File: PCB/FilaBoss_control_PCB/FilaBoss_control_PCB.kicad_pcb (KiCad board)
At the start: 2 copper layers, 81.3 x 53.3 mm, 23 parts, among them J1 Conn_01x04_Encoder, J2 JST_2mm_LiPo, J3 JST_2mm_LiPo, J5 Barrel_Jack_SMD, J6 PinHeader_01x06_P2.54mm_Verti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, J7 Conn_01x04, J8 JST_2mm_3, J9 Conn_01x04_Encoder, Q1 IRLZ44N, Q2 IRLZ44N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

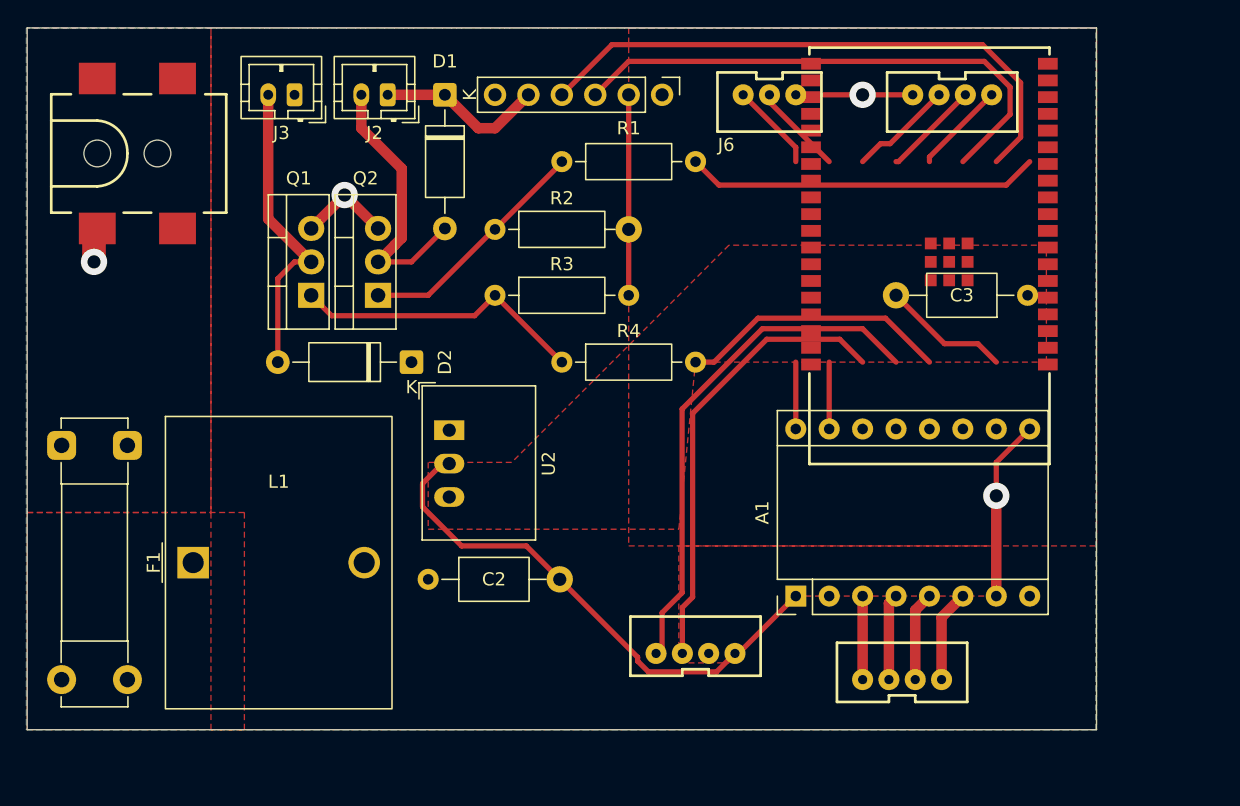
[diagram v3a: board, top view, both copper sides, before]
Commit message: pcb converted to esp32 wroom
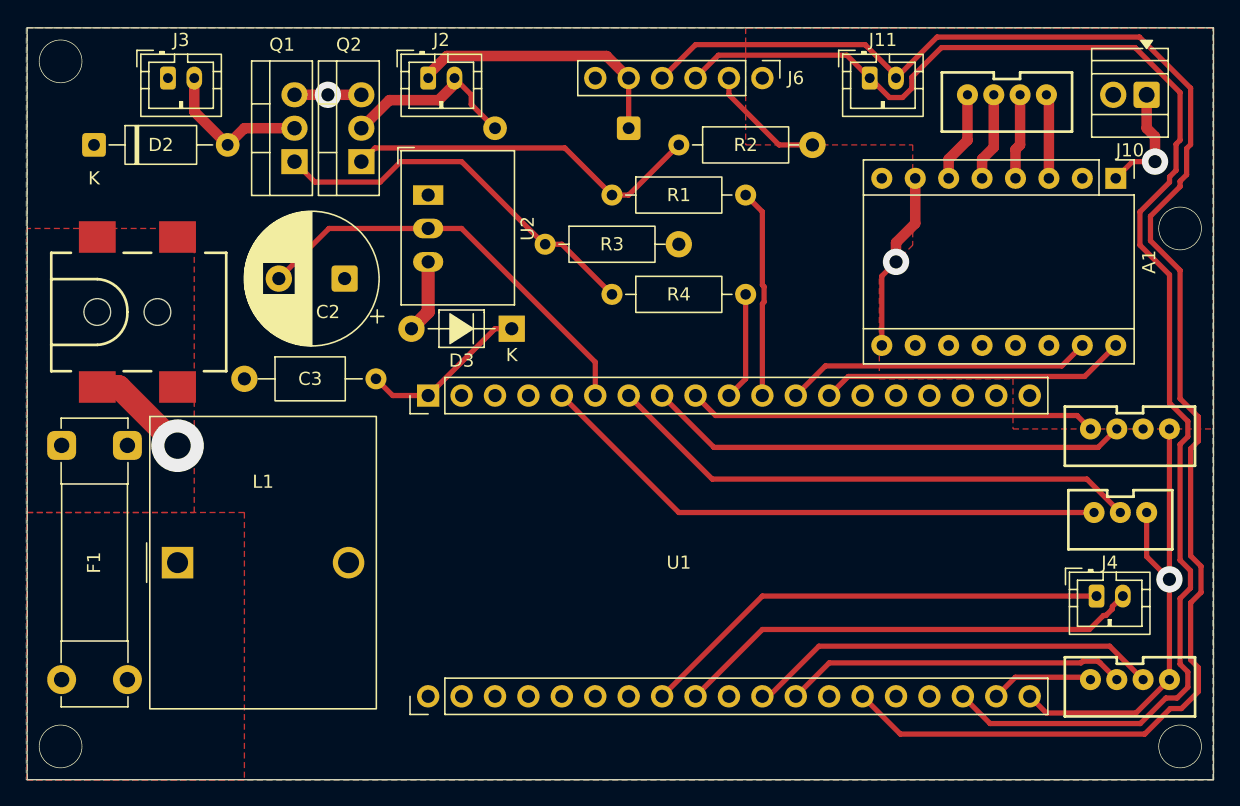
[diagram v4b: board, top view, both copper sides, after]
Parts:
- added D3: SB020, PCM_Diode_THT_AKL:D_T-1_P7.62mm_Horizontal, F.Cu at (74.9, 109.2)
- added J10: Screw_Terminal_01x02, TerminalBlock:TerminalBlock_Xinya_XY308-2.54-2P_1x02_P2.54mm_Horizontal, F.Cu at (123.2, 91.4)
- added J11: SCL/SDA, Connector_JST:JST_PH_B2B-PH-K_1x02_P2.00mm_Vertical, F.Cu at (102.1, 90.2)
- added J4: RX/TX, Connector_JST:JST_PH_B2B-PH-K_1x02_P2.00mm_Vertical, F.Cu at (119.4, 129.5)
- C2: footprint Capacitor_THT:C_Axial_L5.1mm_D3.1mm_P10.00mm_Horizontal -> Capacitor_THT:CP_Radial_D10.0mm_P5.00mm
- D1: moved to B.Cu
- J2: value JST_2mm_LiPo -> SPOOL
- J3: value JST_2mm_LiPo -> PULLER
- J9: value Conn_01x04_Encoder -> Conn_01x04_Pot
- U1: value ESP32-WROVER-E-N16R8 -> ~; footprint PCM_SparkFun-RF:ESP32-WROVER-E-IE -> custom:ESP32 Wroom dev-kit
- moved C3 59.9 mm to (54.6, 113.0), turned to 0 degrees
- moved J9 46.5 mm to (121.9, 136.4)
- moved J7 44.1 mm to (112.6, 92.0), turned to 180 degrees
- moved J8 41.5 mm to (121.2, 123.7)
- moved A1 40.0 mm to (120.8, 97.8), turned to -90 degrees
- moved J1 36.7 mm to (121.9, 117.4), turned to 180 degrees
- moved D2 29.2 mm to (43.2, 95.2), turned to 0 degrees
- moved C2 23.7 mm to (62.2, 105.4), turned to 180 degrees
- moved U2 17.9 mm to (68.6, 99.1)
- moved R2 15.4 mm to (87.6, 95.2)
- moved D1 14.2 mm to (83.8, 94.0), turned to 180 degrees
- moved U1 12.7 mm to (114.3, 114.3)
- moved J5 12.0 mm to (43.4, 108.0)
- moved Q1 10.2 mm to (58.4, 96.5)
- moved Q2 10.2 mm to (63.5, 96.5)
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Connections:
- A1 pad 15: unconnected-(A1-STEP-Pad15) -> Net-(A1-STEP)
- A1 pad 16: GND -> Net-(A1-DIR)
- C3 pad 1: +5V -> GND
- C3 pad 2: unconnected-(C3-Pad2) -> +5V
- J1 pad 1: unconnected-(J1-Pin_1-Pad1) -> GND
- J1 pad 2: unconnected-(J1-Pin_2-Pad2) -> +3.3V
- J1 pad 3: +3.3V -> Net-(J1-Pin_3)
- J1 pad 4: GND -> Net-(J1-Pin_4)
- J6 pad 3: Net-(J6-Pin_3) -> Net-(J11--)
- J6 pad 4: unconnected-(J6-Pin_4-Pad4) -> Net-(J11-+)
- J8 pad 2: unconnected-(J8-Pad2) -> Net-(U1-GPIO12)
- J8 pad 3: unconnected-(J8-Pad3) -> Net-(U1-GPIO13)
- J9 pad 1: Net-(J9-Pin_1) -> GND
- J9 pad 4: GND -> Net-(J9-Pin_4)
- R1 pad 2: unconnected-(R1-Pad2) -> Net-(U1-GPIO25)
- R4 pad 2: unconnected-(R4-Pad2) -> Net-(U1-GPIO26)
- U1 pad 1: Net-(U1-GND-Pad1) -> +5V
- U1 pad 10: unconnected-(U1-IOA25-Pad10) -> Net-(U1-GPIO26)
- U1 pad 11: unconnected-(U1-IOA26-Pad11) -> Net-(U1-GPIO25)
- U1 pad 12: unconnected-(U1-IOA27-Pad12) -> Net-(A1-STEP)
- U1 pad 13: unconnected-(U1-IOA14-Pad13) -> Net-(A1-DIR)
- U1 pad 15: Net-(U1-GND-Pad1) -> unconnected-(U1-GPIO34-Pad15)
- U1 pad 19: unconnected-(U1-NC-Pad19) -> +3.3V
- U1 pad 2: Net-(J6-Pin_3) -> unconnected-(U1-GPIO11-Pad2)
- U1 pad 27: unconnected-(U1-NC-Pad27) -> Net-(J4--)
- U1 pad 28: unconnected-(U1-NC-Pad28) -> Net-(J4-+)
- U1 pad 30: unconnected-(U1-IO18-Pad30) -> Net-(J9-Pin_2)
- U1 pad 31: unconnected-(U1-IO19-Pad31) -> Net-(J9-Pin_3)
- U1 pad 32: unconnected-(U1-NC-Pad32) -> GND
- U1 pad 33: unconnected-(U1-IO21-Pad33) -> Net-(J11-+)
- U1 pad 36: unconnected-(U1-IO22-Pad36) -> Net-(J11--)
- U1 pad 37: unconnected-(U1-IO23-Pad37) -> Net-(J9-Pin_4)
- U1 pad 38: Net-(U1-GND-Pad1) -> GND
- U1 pad 5: unconnected-(U1-IA39-Pad5) -> Net-(U1-GPIO13)
- U1 pad 6: unconnected-(U1-IA34-Pad6) -> GND
- U1 pad 7: unconnected-(U1-IA35-Pad7) -> Net-(U1-GPIO12)
- U1 pad 8: unconnected-(U1-IOA32-Pad8) -> Net-(J1-Pin_3)
- U1 pad 9: unconnected-(U1-IOA33-Pad9) -> Net-(J1-Pin_4)
- U2 pad 3: +5V -> Net-(D3-A)
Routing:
- net Net-(J11-+): track 0.00 -> 123.1 mm
- net Net-(J11--): track 0.00 -> 110.6 mm
- net (no net): track 93.6 -> 0.00 mm, vias 0 -> 4
- net Net-(J6-Pin_3): track 75.1 -> 0.00 mm
- net unconnected-(J6-Pin_4-Pad4): track 44.4 -> 0.00 mm
- net Net-(U1-GPIO13): track 0.00 -> 44.1 mm
- net Net-(U1-GPIO12): track 0.00 -> 41.1 mm
- net Net-(J1-Pin_3): track 0.00 -> 36.8 mm
- net Net-(J4--): track 0.00 -> 36.2 mm
- net Net-(J4-+): track 0.00 -> 35.7 mm
- net Net-(J1-Pin_4): track 0.00 -> 31.1 mm
- net Net-(J9-Pin_2): track 7.56 -> 31.6 mm
- net Net-(A1-STEP): track 0.00 -> 23.4 mm
- net Net-(A1-DIR): track 0.00 -> 23.4 mm
- net GND: track 93.3 -> 114.3 mm, vias 4 -> 5
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- removed copper zone on F.Cu, net +5V
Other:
- board size 81.3 x 53.3 mm -> 90.2 x 57.2 mm

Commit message: pcb-schematic
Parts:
- added J12: Screw_Terminal_01x02, TerminalBlock:TerminalBlock_Xinya_XY308-2.54-2P_1x02_P2.54mm_Horizontal, F.Cu at (90.2, 144.8)
- added J13: Screw_Terminal_01x02, TerminalBlock:TerminalBlock_Xinya_XY308-2.54-2P_1x02_P2.54mm_Horizontal, F.Cu at (64.8, 144.8)
- added J14: Conn_01x04_Encoder, Connector_JST:JST_XA_B04B-XASK-1_1x04_P2.50mm_Vertical, F.Cu at (102.9, 144.8)
- added U3: R-78B12-2.0, Converter_DCDC:Converter_DCDC_RECOM_R-78B-2.0_THT, F.Cu at (76.2, 142.2)
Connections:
- U1 pad 26: unconnected-(U1-GPIO4-Pad26) -> Net-(J14-Pin_3)
- U1 pad 29: unconnected-(U1-GPIO5-Pad29) -> Net-(J14-Pin_4)
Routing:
- net GND: track 114.3 -> 162.4 mm, vias 5 -> 6
- net +5V: track 13.0 -> 45.0 mm
- net Net-(J14-Pin_3): track 0.00 -> 27.2 mm
- net Net-(J14-Pin_4): track 0.00 -> 22.1 mm
- added copper zone on F.Cu, net +12V
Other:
- board size 90.2 x 57.2 mm -> 90.2 x 63.5 mm

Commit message: pcb
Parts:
- F1: footprint Fuse:Fuseholder_Clip-5x20mm_Bel_FC-203-22_Lateral_P17.80x5.00mm_D1.17mm_Horizontal -> Fuse:Fuseholder_Clip-5x20mm_Littelfuse_521_Lateral_P17.00x5.00mm_D1.30mm_Horizontal
- moved C3 25.8 mm to (79.9, 118.1), turned to 180 degrees
- moved L1 11.4 mm to (49.5, 138.4)
- moved F1 6.76 mm to (45.7, 124.8)
- moved J9 5.09 mm to (122.2, 141.5)
- moved J4 5.08 mm to (119.4, 134.6)
- moved J5 4.61 mm to (42.2, 112.4)
- moved J8 2.64 mm to (121.9, 121.2)
- moved J12 2.54 mm to (87.6, 144.8)
- moved J13 2.54 mm to (67.3, 144.8)
- moved J1 1.82 mm to (121.9, 115.6)
- moved J7 0.55 mm to (112.6, 91.4)
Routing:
- net GND: track 162.4 -> 0.00 mm, vias 6 -> 5
- net Net-(J11-+): track 123.1 -> 0.00 mm
- net Net-(J11--): track 110.6 -> 0.00 mm
- net +5V: track 45.0 -> 0.00 mm
- net Net-(U1-GPIO13): track 44.1 -> 0.00 mm
- net Net-(U1-GPIO12): track 41.1 -> 0.00 mm
- net Net-(J1-Pin_3): track 36.8 -> 0.00 mm
- net Net-(J4--): track 36.2 -> 0.00 mm
- net Net-(J4-+): track 35.7 -> 0.00 mm
- net Net-(J9-Pin_2): track 31.6 -> 0.00 mm
- net Net-(J1-Pin_4): track 31.1 -> 0.00 mm
- net Net-(Q1-G): track 29.6 -> 0.00 mm
- net Net-(Q2-G): track 27.9 -> 0.00 mm
- net Net-(J14-Pin_3): track 27.2 -> 0.00 mm
- net Net-(J9-Pin_3): track 26.1 -> 0.00 mm
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- added copper zone on B.Cu, net +12V
- added copper zone on B.Cu, net +24V
- added copper zone on B.Cu, net +3.3V
- added copper zone on F.Cu, net GND
- added copper zone on B.Cu, net LINE
- added copper zone on B.Cu, net VDC
- removed copper zone on F.Cu, net +12V
- removed copper zone on F.Cu, net +24V
- removed copper zone on F.Cu, net +3.3V
- removed copper zone on B.Cu, net GND
- removed copper zone on F.Cu, net LINE
- removed copper zone on F.Cu, net VDC

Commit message: pcb
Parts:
- added OC1: H11A1, PCM_Package_DIP_AKL:DIP-6_W7.62mm_LongPads, F.Cu at (164.8, 79.5)
- added OC2: H11A1, PCM_Package_DIP_AKL:DIP-6_W7.62mm_LongPads, F.Cu at (164.8, 88.7)
- added R10: 330R, Resistor_THT:R_Axial_DIN0207_L6.3mm_D2.5mm_P10.16mm_Horizontal, F.Cu at (151.1, 99.7)
- added R11: 330R, Resistor_THT:R_Axial_DIN0207_L6.3mm_D2.5mm_P10.16mm_Horizontal, F.Cu at (151.1, 103.7)
- added R12: 4.7k, Resistor_THT:R_Axial_DIN0207_L6.3mm_D2.5mm_P10.16mm_Horizontal, F.Cu at (151.1, 107.8)
- added R13: 4.7k, Resistor_THT:R_Axial_DIN0207_L6.3mm_D2.5mm_P10.16mm_Horizontal, F.Cu at (151.1, 111.8)
- added R14: 4.7k, Resistor_THT:R_Axial_DIN0207_L6.3mm_D2.5mm_P10.16mm_Horizontal, F.Cu at (151.1, 115.9)
- added R15: 4.7k, Resistor_THT:R_Axial_DIN0207_L6.3mm_D2.5mm_P10.16mm_Horizontal, F.Cu at (151.1, 119.9)
- added R16: 4.7k, Resistor_THT:R_Axial_DIN0207_L6.3mm_D2.5mm_P10.16mm_Horizontal, F.Cu at (151.1, 124.0)
- added R17: 4.7k, Resistor_THT:R_Axial_DIN0207_L6.3mm_D2.5mm_P10.16mm_Horizontal, F.Cu at (151.1, 128.0)
- added R18: 4.7k, Resistor_THT:R_Axial_DIN0207_L6.3mm_D2.5mm_P10.16mm_Horizontal, F.Cu at (73.7, 141.0)
- added R5: 100R, Resistor_THT:R_Axial_DIN0207_L6.3mm_D2.5mm_P10.16mm_Horizontal, F.Cu at (151.1, 79.4)
- added R6: 100R, Resistor_THT:R_Axial_DIN0207_L6.3mm_D2.5mm_P10.16mm_Horizontal, F.Cu at (151.1, 83.5)
- added R7: 100R, Resistor_THT:R_Axial_DIN0207_L6.3mm_D2.5mm_P10.16mm_Horizontal, F.Cu at (151.1, 87.5)
- added R8: 100R, Resistor_THT:R_Axial_DIN0207_L6.3mm_D2.5mm_P10.16mm_Horizontal, F.Cu at (151.1, 91.6)
- added R9: 100R, Resistor_THT:R_Axial_DIN0207_L6.3mm_D2.5mm_P10.16mm_Horizontal, F.Cu at (151.1, 95.6)
- J1: value Conn_01x04_Encoder -> Encoder
- J10: value Screw_Terminal_01x02 -> Power 3.3v
- J12: value Screw_Terminal_01x02 -> power 12v
- J13: value Screw_Terminal_01x02 -> power 5v
- J14: value Conn_01x04_Encoder -> Fan connector
- J6: value PinHeader_01x06_P2.54mm_Vertical_THT_D1mm -> INA219
- J7: value Conn_01x04 -> Stepper
- J8: value JST_2mm_3 -> limit switch
- moved U1 33.1 mm to (86.4, 132.1)
- moved U3 28.1 mm to (54.7, 160.4)
- moved J13 27.2 mm to (45.7, 161.3)
- moved J12 27.2 mm to (66.0, 161.3)
- moved D2 18.0 mm to (52.8, 80.0)
- moved J3 18.0 mm to (58.4, 74.9)
- moved F1 15.6 mm to (45.7, 109.2)
- moved J14 15.2 mm to (102.9, 160.0)
- moved J9 15.2 mm to (122.2, 156.8)
- moved L1 14.5 mm to (58.4, 127.0), turned to 90 degrees
- moved J5 14.0 mm to (42.2, 98.4)
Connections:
- J1 pad 2: +3.3V -> +5V
- J2 pad 1: Net-(D1-K) -> Net-(D1-A)
- J2 pad 2: Net-(D1-A) -> Net-(D1-K)
- J3 pad 1: +24V -> Net-(D2-A)
- J3 pad 2: Net-(D2-A) -> +24V
- J8 pad 1: GND -> Net-(J8-Pad1)
- J8 pad 2: Net-(U1-GPIO12) -> Net-(J8-Pad2)
- J8 pad 3: Net-(U1-GPIO13) -> GND
- U1 pad 24: unconnected-(U1-GPIO2-Pad24) -> Net-(J14-Pin_4)
- U1 pad 25: unconnected-(U1-GPIO0-Pad25) -> Net-(J14-Pin_3)
- U1 pad 26: Net-(J14-Pin_3) -> unconnected-(U1-GPIO4-Pad26)
- U1 pad 29: Net-(J14-Pin_4) -> Net-(U1-GPIO5)
- U1 pad 30: Net-(J9-Pin_2) -> Net-(U1-GPIO18)
- U1 pad 31: Net-(J9-Pin_3) -> Net-(U1-GPIO19)
- U1 pad 37: Net-(J9-Pin_4) -> unconnected-(U1-GPIO23-Pad37)
- U1 pad 8: Net-(J1-Pin_3) -> Net-(U1-GPIO14)
- U1 pad 9: Net-(J1-Pin_4) -> Net-(U1-GPIO27)
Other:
- board size 90.2 x 63.5 mm -> 90.2 x 78.7 mm

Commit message: :/
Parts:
- removed OC1, OC2: H11A1, PCM_Package_DIP_AKL:DIP-6_W7.62mm_LongPads
- removed R10, R11: 330R, Resistor_THT:R_Axial_DIN0207_L6.3mm_D2.5mm_P10.16mm_Horizontal
- removed R12, R13: 4.7k, Resistor_THT:R_Axial_DIN0207_L6.3mm_D2.5mm_P10.16mm_Horizontal
- removed U3: R-78B12-2.0, Converter_DCDC:Converter_DCDC_RECOM_R-78B-2.0_THT
- added J15: power 12v, TerminalBlock:TerminalBlock_Xinya_XY308-2.54-2P_1x02_P2.54mm_Horizontal, F.Cu at (68.6, 172.7)
- added J16: Screen, Connector_JST:JST_PH_B4B-PH-K_1x04_P2.00mm_Vertical, F.Cu at (132.7, 162.1)
- added U4: R-78E12-2, Converter_DCDC:Converter_DCDC_RECOM_R-78E-0.5_THT, F.Cu at (85.4, 160.1)
- D1: moved to F.Cu
- D3: footprint PCM_Diode_THT_AKL:D_T-1_P7.62mm_Horizontal -> Diode_THT:D_A-405_P10.16mm_Horizontal
- J1, J9: footprint PCM_SparkFun-Connector:JST_1x04_P2.0mm_Vertical_PTH -> Connector_JST:JST_PH_B4B-PH-K_1x04_P2.00mm_Vertical
- J2, J3: footprint Connector_JST:JST_PH_B2B-PH-K_1x02_P2.00mm_Vertical -> Connector_JST:JST_XA_B02B-XASK-1_1x02_P2.50mm_Vertical
- J7: footprint PCM_SparkFun-Connector:JST_1x04_P2.0mm_Vertical_PTH -> Connector_JST:JST_XA_B04B-XASK-1_1x04_P2.50mm_Vertical
- J8: footprint PCM_SparkFun-Connector:JST_1x03_P2.0mm_Vertical_PTH -> Connector_JST:JST_PH_B3B-PH-K_1x03_P2.00mm_Vertical
- moved J13 70.8 mm to (115.6, 172.7)
- moved D3 68.4 mm to (114.3, 165.1)
- moved J11 68.0 mm to (133.3, 150.6), turned to 90 degrees
- moved R18 67.6 mm to (135.3, 113.0), turned to -90 degrees
- moved U2 66.6 mm to (95.2, 160.1)
- moved J3 66.5 mm to (43.2, 139.7), turned to 90 degrees
- moved F1 60.4 mm to (45.1, 169.6), turned to 0 degrees
- moved D2 60.0 mm to (58.4, 139.7), turned to 180 degrees
- moved J5 58.4 mm to (41.8, 156.8)
- moved J1 58.2 mm to (129.5, 173.3)
- moved R6 57.3 mm to (109.9, 123.2), turned to 90 degrees
- moved J9 57.1 mm to (114.1, 100.2)
- moved C2 55.5 mm to (77.5, 158.8), turned to -90 degrees
- moved R5 52.3 mm to (122.6, 123.2), turned to 90 degrees
- moved R7 49.9 mm to (116.2, 123.2), turned to 90 degrees
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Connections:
- J14 pad 1: GND -> Net-(J14-Pin_1)
- J14 pad 2: +12V -> Net-(J14-Pin_2)
- J14 pad 3: Net-(J14-Pin_3) -> +12V
- J14 pad 4: Net-(J14-Pin_4) -> GND
- R1 pad 2: Net-(U1-GPIO25) -> Net-(U1-GPIO26)
- R4 pad 2: Net-(U1-GPIO26) -> Net-(U1-GPIO25)
- R8 pad 2: Net-(U1-GPIO13) -> Net-(U1-GPIO35)
- R9 pad 2: Net-(U1-GPIO12) -> Net-(U1-GPIO34)
- U1 pad 12: Net-(A1-STEP) -> Net-(J14-Pin_1)
- U1 pad 13: Net-(A1-DIR) -> Net-(J14-Pin_2)
- U1 pad 14: unconnected-(U1-GPIO35-Pad14) -> Net-(U1-GPIO35)
- U1 pad 15: unconnected-(U1-GPIO34-Pad15) -> Net-(U1-GPIO34)
- U1 pad 23: unconnected-(U1-GPIO15-Pad23) -> Net-(A1-STEP)
- U1 pad 24: Net-(J14-Pin_4) -> Net-(A1-DIR)
- U1 pad 25: Net-(J14-Pin_3) -> unconnected-(U1-GPIO0-Pad25)
- U1 pad 5: Net-(U1-GPIO13) -> unconnected-(U1-GPIO13-Pad5)
- U1 pad 7: Net-(U1-GPIO12) -> unconnected-(U1-GPIO12-Pad7)
- U1 pad 8: Net-(U1-GPIO14) -> Net-(J1-Pin_3)
- U1 pad 9: Net-(U1-GPIO27) -> Net-(J1-Pin_4)
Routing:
- net Net-(J11--): track 0.00 -> 83.1 mm
- net Net-(J11-+): track 0.00 -> 82.6 mm
- net Net-(D1-K): track 0.00 -> 42.1 mm
- net Net-(A1-STEP): track 0.00 -> 41.0 mm
- net Net-(A1-DIR): track 0.00 -> 36.4 mm
- net Net-(J14-Pin_2): track 0.00 -> 33.0 mm
- net Net-(J14-Pin_1): track 0.00 -> 31.6 mm
- net Net-(J4-+): track 0.00 -> 30.2 mm
- net Net-(J1-Pin_4): track 0.00 -> 28.4 mm
- net Net-(J1-Pin_3): track 0.00 -> 28.2 mm
- net Net-(U1-GPIO26): track 0.00 -> 27.4 mm
- net Net-(J4--): track 0.00 -> 27.3 mm
- net Net-(U1-GPIO25): track 0.00 -> 23.4 mm
- net Net-(U1-GPIO5): track 0.00 -> 22.3 mm
- net Net-(J8-Pad1): track 0.00 -> 18.5 mm
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- added copper zone on B.Cu, net +5V
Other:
- board size 90.2 x 78.7 mm -> 101.6 x 80 mm
